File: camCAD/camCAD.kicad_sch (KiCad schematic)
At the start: 0 parts

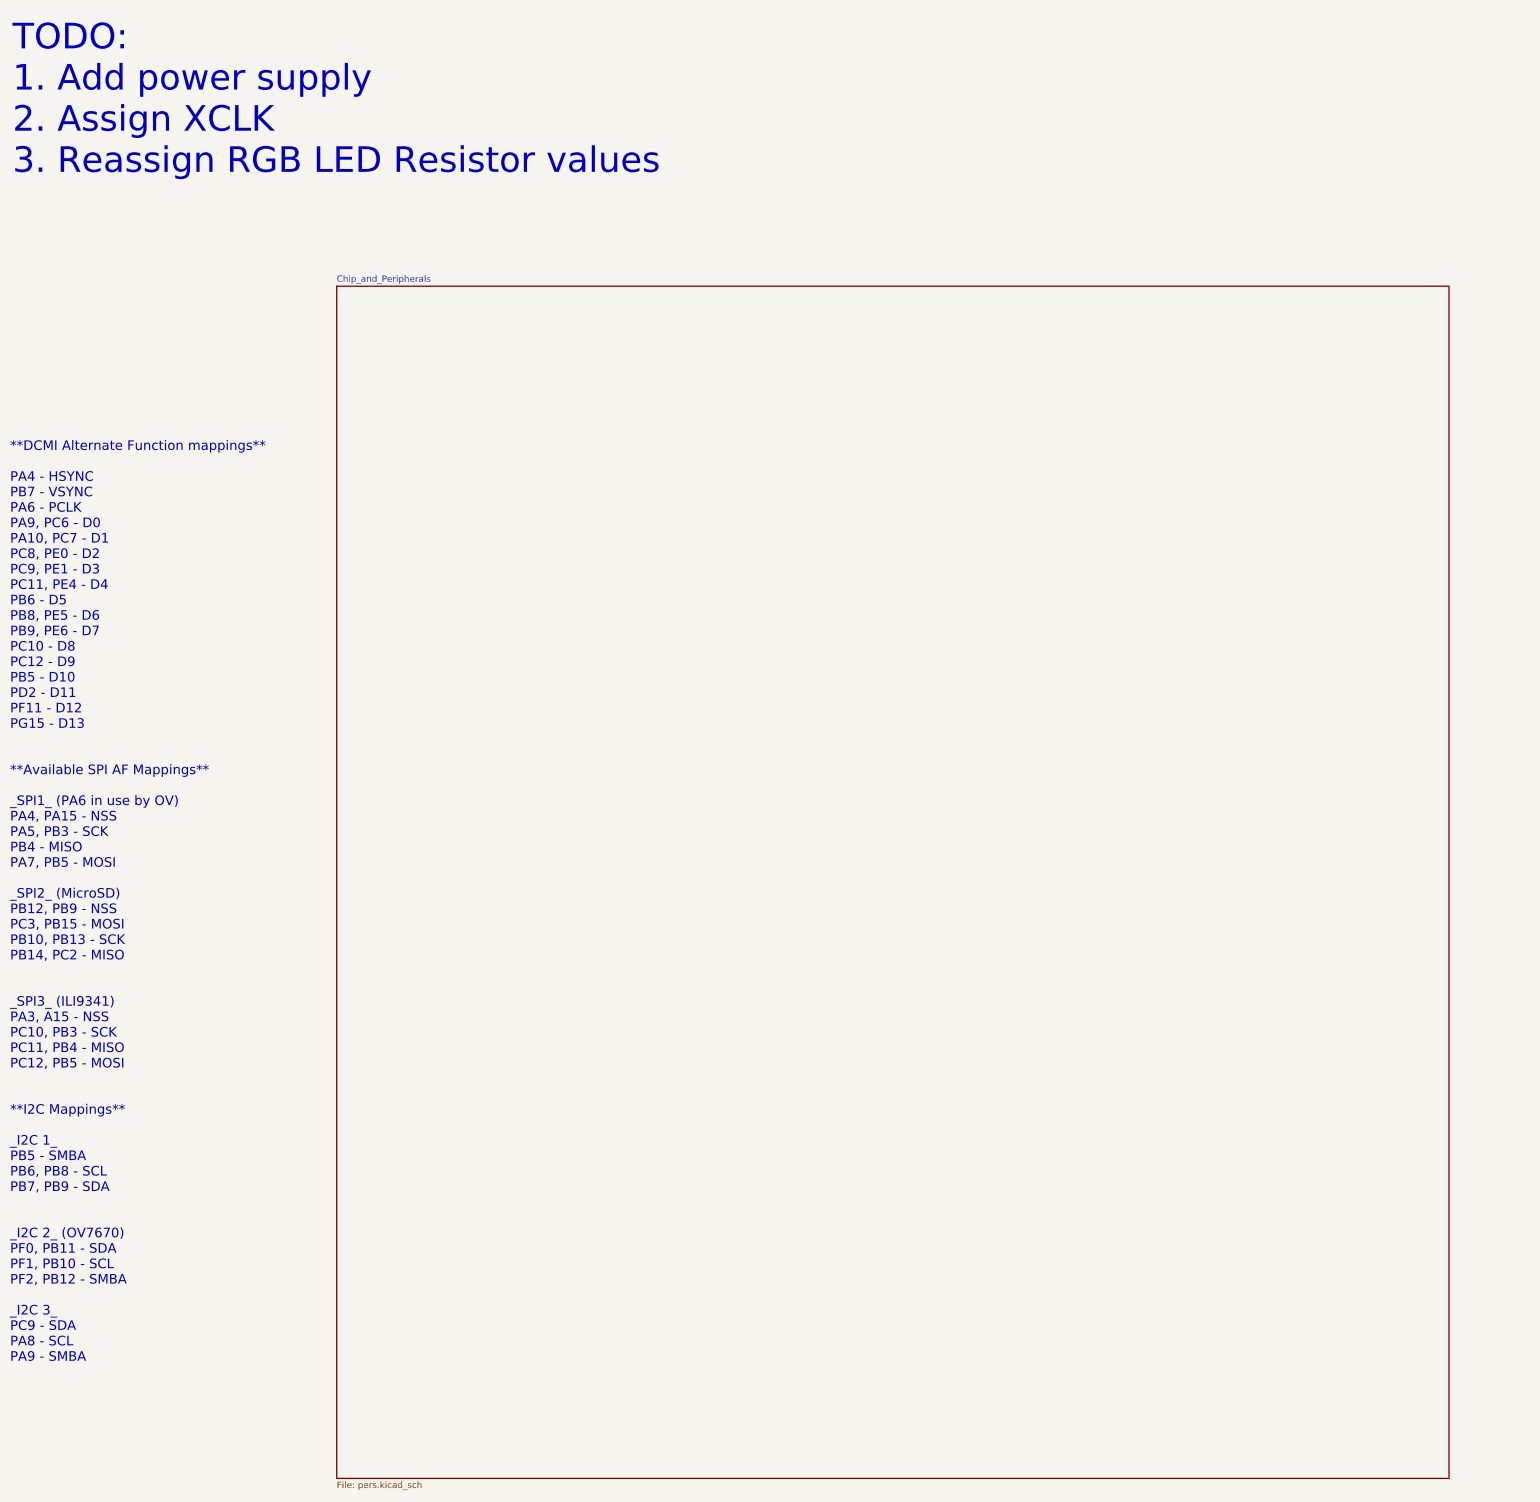
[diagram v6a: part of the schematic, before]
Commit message: restructured hierarchy and cleaned up schematic
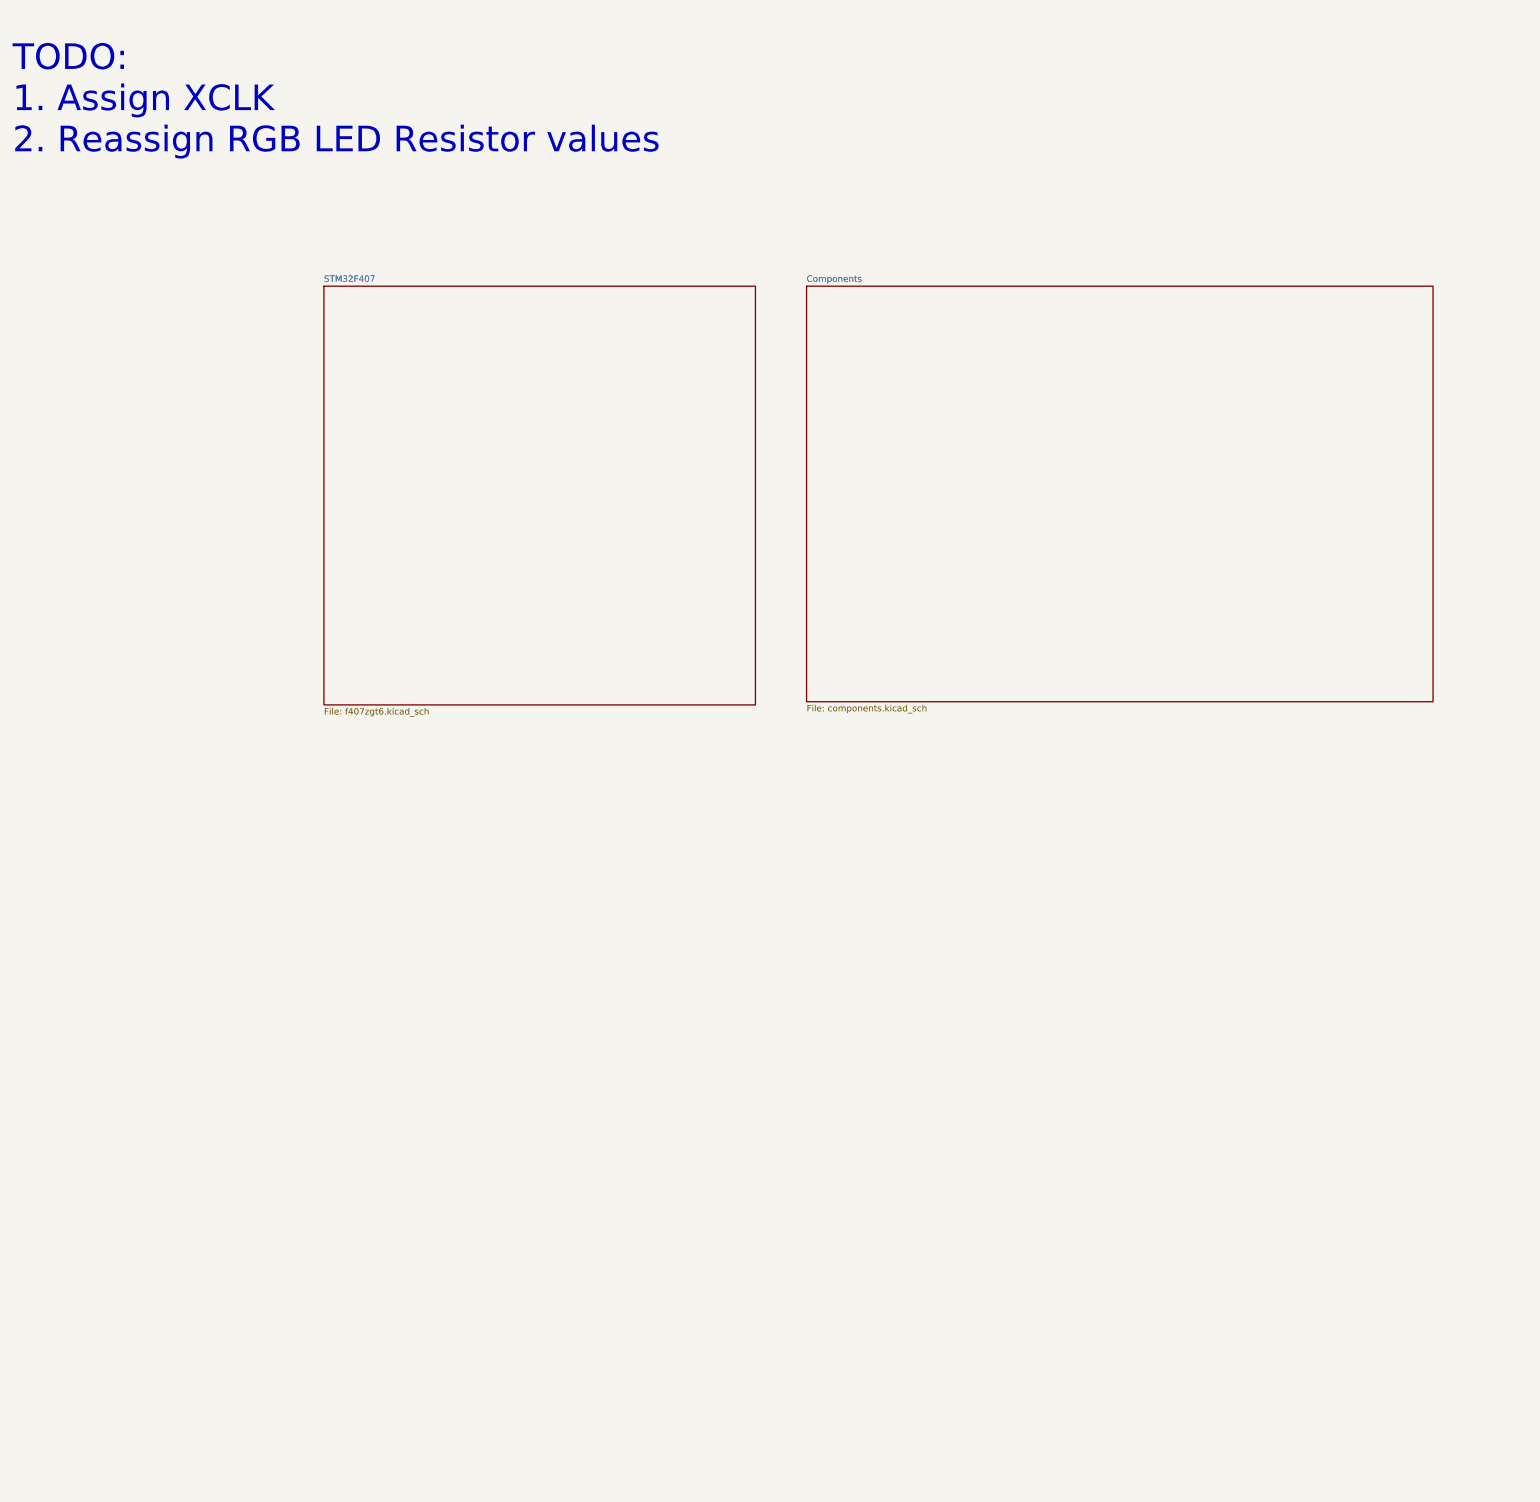
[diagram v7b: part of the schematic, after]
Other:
- removed sheet Chip_and_Peripherals
- added sheet Components (components.kicad_sch)
- added sheet STM32F407 (f407zgt6.kicad_sch)
- note added: "TODO: 1. Assign XCLK 2. Reassign RGB LED Resistor values"
- note removed: "**DCMI Alternate Function mappings** PA4 - HSYNC PB7 - VSYNC PA6 - PCLK PA9, PC6 - D0 PA10, PC7 - D1 PC8, PE0 - D2 PC9, PE1 - D3 PC11, PE4 - D4 PB6 - D5 PB8, PE5 - D6 PB9, PE6 - D7 PC10 - D8 PC12 - D9 PB5 - D10 PD2 - D11 PF11 - D12 PG15 - D13 **Available SPI AF Mappings** _SPI1_ (PA6 in use by OV) PA4, PA15 - NSS PA5, PB3 - SCK PB4 - MISO PA7, PB5 - MOSI _SPI2_ (MicroSD) PB12, PB9 - NSS PC3, PB15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"
- note removed: "TODO: 1. Add power supply 2. Assign XCLK 3. Reassign RGB LED Resistor values"
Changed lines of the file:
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@@
 	(generator_version "10.0")
 	(paper "A2")
-	(text "**DCMI Alternate Function mappings**\n\nPA4 - HSYNC \nPB7 - VSYNC \nPA6 - PCLK \nPA9, PC6 - D0 \nPA10, PC7 - D1\nPC8, PE0 - D2\nPC9, PE1 - D3\nPC11, PE4 - D4\nPB6 - D5 \nPB8, PE5 - D6\nPB9, PE6 - D7\nPC10 - D8 \nPC12 - D9\nPB5 - D10\nPD2 - D11\nPF11 - D12\nPG15 - D13\n\n\n**Available SPI AF Mappings**\n\n_SPI1_ (PA6 in use by OV)\nPA4, PA15 - NSS\nPA5, PB3 - SCK\nPB4 - MISO\nPA7, PB5 - MOSI\n\n_SPI2_ (MicroSD)\nPB12, PB9 - NSS\nPC3, PB15 - MOSI\nPB10, PB13 - SCK\nPB14, PC2 - MISO\n\n\n_SPI3_ (ILI9341)\nPA3, A15 - NSS\nPC10, PB3 - SCK\nPC11, PB4 - MISO\nPC12, PB5 - MOSI\n\n\n**I2C Mappings**\n\n_I2C 1_\nPB5 - SMBA\nPB6, PB8 - SCL\nPB7, PB9 - SDA\n\n\n_I2C 2_ (OV7670)\nPF0, PB11 - SDA\nPF1, PB10 - SCL\nPF2, PB12 - SMBA\n\n_I2C 3_ \nPC9 - SDA\nPA8 - SCL\nPA9 - SMBA\n\n\n\n\n\n"
-		(exclude_from_sim no)
-		(at 23.368 207.518 0)
-		(effects
-			(font
-				(size 1.905 1.905)
-			)
-			(justify left)
-		)
-	)
-	(text "TODO:\n1. Add power supply\n2. Assign XCLK\n3. Reassign RGB LED Resistor values\n"
+	(text "TODO:\n1. Assign XCLK\n2. Reassign RGB LED Resistor values\n"
 		(exclude_from_sim no)
 		(at 23.876 40.386 0)
@@
 	)
 	(sheet
-		(at 88.265 77.47)
-		(size 220.98 236.855)
+		(at 85.725 77.47)
+		(size 85.725 83.185)
 		(exclude_from_sim no)
 		(in_bom yes)
@@
 			(color 0 0 0 0)
 		)
-		(property "Sheetname" "Chip_and_Peripherals"
-			(at 88.265 76.7584 0)
+		(property "Sheetname" "STM32F407"
+			(at 85.725 76.7584 0)
 			(show_name no)
 			(do_not_autoplace no)
@@
 			)
 		)
-		(property "Sheetfile" "pers.kicad_sch"
-			(at 88.265 314.9096 0)
+		(property "Sheetfile" "f407zgt6.kicad_sch"
+			(at 85.725 161.2396 0)
 			(show_name no)
 			(do_not_autoplace no)
@@
 			(project "camCAD"
 				(path "/e2824ea6-9024-4cee-b80c-5fefbc7112d7"
-					(page "3")
+					(page "5")
 				)
 			)
+		)
+	)
+	(sheet
+		(at 181.61 77.47)
+		(size 124.46 82.55)
+		(exclude_from_sim no)
+		(in_bom yes)
+		(on_board yes)
+		(dnp no)
+		(fields_autoplaced yes)
+		(stroke
+			(width 0.1524)
+			(type solid)
+		)
+		(fill
+			(color 0 0 0 0)
+		)
+		(property "Sheetname" "Components"
+			(at 181.61 76.7584 0)
+			(show_name no)
+			(do_not_autoplace no)
+			(effects
+				(font
+					(size 1.27 1.27)
+				)
+				(justify left bottom)
+			)
+		)
+		(property "Sheetfile" "components.kicad_sch"
+			(at 181.61 160.6046 0)
+			(show_name no)
+			(do_not_autoplace no)
+			(effects
+				(font
+					(size 1.27 1.27)
+				)
+				(justify left top)
+			)
+		)
+		(instances
+			(project "camCAD"
+				(path "/e2824ea6-9024-4cee-b80c-5fefbc7112d7"
+					(page "6")
+				)
+			)

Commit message: Added battery to HardwareNotes.md, some touch ups on schematic
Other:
- note added: "TODO: 1. Assign XCLK to TIM 2. Reassign RGB LED Resistor values 3. Create a charging / data port (USBC)"
- note removed: "TODO: 1. Assign XCLK 2. Reassign RGB LED Resistor values"
- title: (none) -> Root for camCAD
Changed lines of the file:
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@@
 	(generator "eeschema")
 	(generator_version "10.0")
-	(paper "A2")
-	(text "TODO:\n1. Assign XCLK\n2. Reassign RGB LED Resistor values\n"
+	(paper "User" 381 279.4)
+	(title_block
+		(title "Root for camCAD")
+		(date "2026-06-11")
+		(rev "Jun26")
+		(comment 4 "By Siddharth Vasudevan")
+	)
+	(text "TODO:\n1. Assign XCLK to TIM\n2. Reassign RGB LED Resistor values\n3. Create a charging / data port (USBC)\n"
 		(exclude_from_sim no)
-		(at 23.876 40.386 0)
+		(at 245.364 47.752 0)
 		(effects
 			(font
-				(size 5.08 5.08)
+				(size 3.81 3.81)
 			)
 			(justify left)
@@
 	)
 	(sheet
-		(at 85.725 77.47)
-		(size 85.725 83.185)
+		(at 25.4 29.21)
+		(size 85.725 100.965)
 		(exclude_from_sim no)
 		(in_bom yes)
@@
 		)
 		(property "Sheetname" "STM32F407"
-			(at 85.725 76.7584 0)
+			(at 25.4 28.4984 0)
 			(show_name no)
 			(do_not_autoplace no)
@@
 		)
 		(property "Sheetfile" "f407zgt6.kicad_sch"
-			(at 85.725 161.2396 0)
+			(at 25.4 130.7596 0)
+			(show_name no)
+			(do_not_autoplace no)
+			(effects
+				(font
+					(size 1.27 1.27)
+				)
+				(justify left top)
+			)
+		)
+		(instances
+			(project "camCAD"
+				(path "/e2824ea6-9024-4cee-b80c-5fefbc7112d7"
+					(page "2")
+				)
+			)
+		)
+	)
+	(sheet
+		(at 129.54 29.21)
+		(size 101.6 100.965)
+		(exclude_from_sim no)
+		(in_bom yes)
+		(on_board yes)
+		(dnp no)
+		(fields_autoplaced yes)
+		(stroke
+			(width 0.1524)
+			(type solid)
+		)
+		(fill
+			(color 0 0 0 0)
+		)
+		(property "Sheetname" "Components"
+			(at 129.54 28.4984 0)
+			(show_name no)
+			(do_not_autoplace no)
+			(effects
+				(font
+					(size 1.27 1.27)
+				)
+				(justify left bottom)
+			)
+		)
+		(property "Sheetfile" "components.kicad_sch"
+			(at 129.54 130.7596 0)
 			(show_name no)
 			(do_not_autoplace no)
@@
 	)
 	(sheet
-		(at 181.61 77.47)
-		(size 124.46 82.55)
-		(exclude_from_sim no)
-		(in_bom yes)
-		(on_board yes)
-		(dnp no)
-		(fields_autoplaced yes)
-		(stroke
-			(width 0.1524)
-			(type solid)
-		)
-		(fill
-			(color 0 0 0 0)
-		)
-		(property "Sheetname" "Components"
-			(at 181.61 76.7584 0)
-			(show_name no)
-			(do_not_autoplace no)
-			(effects
-				(font
-					(size 1.27 1.27)
-				)
-				(justify left bottom)
-			)
-		)
-		(property "Sheetfile" "components.kicad_sch"
-			(at 181.61 160.6046 0)
-			(show_name no)
-			(do_not_autoplace no)
-			(effects
-				(font
-					(size 1.27 1.27)
-				)
-				(justify left top)
-			)
-		)
-		(instances
-			(project "camCAD"
-				(path "/e2824ea6-9024-4cee-b80c-5fefbc7112d7"
-					(page "6")
-				)
-			)
-		)
-	)
-	(sheet
-		(at 338.455 236.855)
-		(size 213.995 77.47)
+		(at 129.54 149.86)
+		(size 102.235 96.52)
 		(exclude_from_sim no)
 		(in_bom yes)
@@
 		)
 		(property "Sheetname" "Buck_Converter"
-			(at 338.455 236.1434 0)
+			(at 129.54 149.1484 0)
 			(show_name no)
 			(do_not_autoplace no)
@@
 		)
 		(property "Sheetfile" "buck.kicad_sch"
-			(at 338.455 314.9096 0)
+			(at 129.54 246.9646 0)
 			(show_name no)
 			(do_not_autoplace no)
@@
 	)
 	(sheet
-		(at 337.82 76.835)
-		(size 215.265 142.24)
+		(at 26.035 149.225)
+		(size 84.455 95.885)
 		(exclude_from_sim no)
 		(in_bom yes)
@@
 		)
 		(property "Sheetname" "Power_Supply_Scheme"
-			(at 337.82 76.1234 0)
+			(at 26.035 148.5134 0)
 			(show_name no)
 			(do_not_autoplace no)
@@
 		)
 		(property "Sheetfile" "power_conns.kicad_sch"
-			(at 337.82 219.6596 0)
+			(at 26.035 245.6946 0)
 			(show_name no)
 			(do_not_autoplace no)
@@
 			(project "camCAD"
 				(path "/e2824ea6-9024-4cee-b80c-5fefbc7112d7"
-					(page "2")
+					(page "3")
 				)
 			)
